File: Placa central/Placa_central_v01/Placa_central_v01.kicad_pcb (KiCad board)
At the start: 2 copper layers, 28 parts, among them J1 Conn_8.4V_PlacaAlimentação, J2 Conn_01x02_ArduinoTxRx, J26 Conn_02x08_Odd_Even, J3 Conn_01x01_ArduinoReset, J37 Conn_01x01_8.4VPonteH, J38 Conn_01x01_5VPonteH, J39 Conn_01x01_GNDPonteH, J4 Conn_GND_PlacaAlimentação, J40 Conn_01x01_Motor1PWM, J41 Conn_01x01_Motor1Dir1, J42 Conn_01x01_Motor1Dir2, J43 Conn_01x01_Motor2Dir1, J44 Conn_01x01_Motor2Dir2, J45 Conn_01x01_Motor2PWM, J48 Conn_01x01_5VEncoderEsq, J49 Conn_01x01_OutputEncoderEsq, J50 Conn_01x01_GNDEncoderEsq, J51 Conn_01x01_5VEncoderDir, J52 Conn_01x01_OutputEncoderDir, J53 Conn_01x01_GNDEncoderDir, SW3 SW_comando1

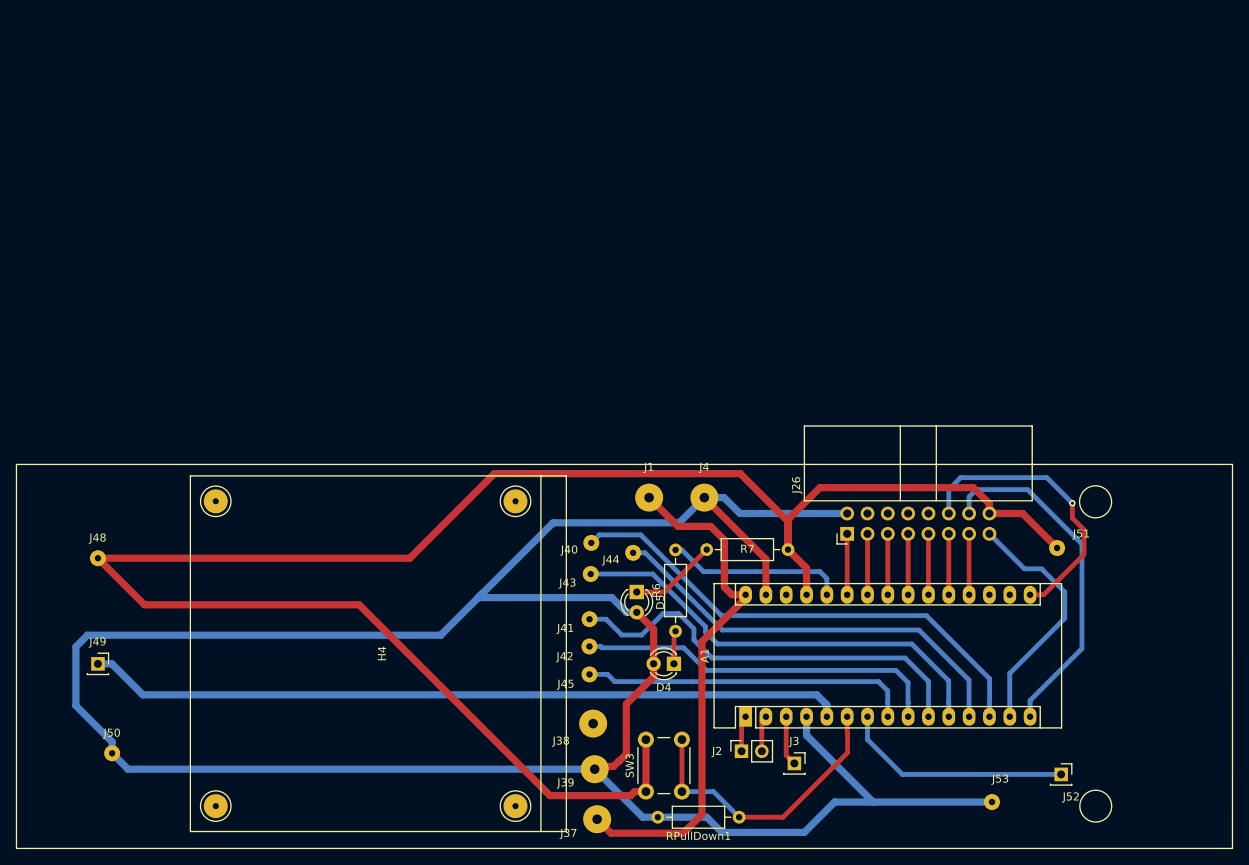
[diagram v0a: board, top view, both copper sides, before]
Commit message: Adicionada a zona de malha de ground, furos pendentes.
A zona de ground ainda não foi preenchida pois os furos da placa para fixação no acrílico requerem atualização.
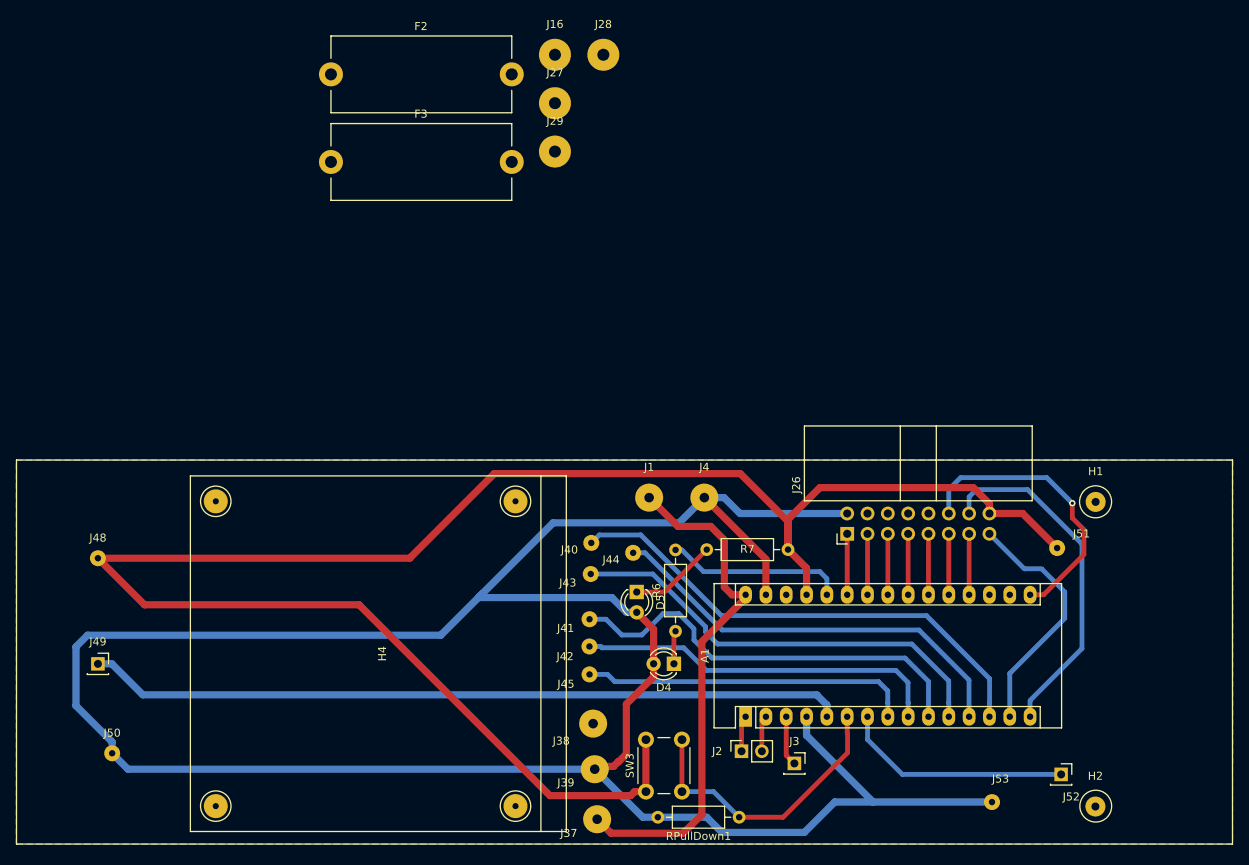
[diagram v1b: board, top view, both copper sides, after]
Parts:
- added F2: Fuse-3A, Fuse:Fuseholder_Cylinder-5x20mm_Stelvio-Kontek_PTF78_Horizontal_Open, F.Cu at (63.9, 74.4)
- added F3: Fuse-3A, Fuse:Fuseholder_Cylinder-5x20mm_Stelvio-Kontek_PTF78_Horizontal_Open, F.Cu at (63.9, 85.3)
- added H1: FuroPlaca, Connector_Wire:SolderWirePad_1x01_Drill1mm, F.Cu at (159.5, 127.8)
- added H2: FuroPlaca, Connector_Wire:SolderWirePad_1x01_Drill1mm, F.Cu at (159.5, 165.9)
- added J16: Conn_01x01_Motor1PonteHPCB, Connector_Wire:SolderWirePad_1x01_Drill1.5mm, F.Cu at (91.9, 71.9)
- added J27: Conn_01x01_Motor2PonteHPCB, Connector_Wire:SolderWirePad_1x01_Drill1.5mm, F.Cu at (91.9, 78.0)
- added J28: Conn_01x01_Motor1PCBMotor, Connector_Wire:SolderWirePad_1x01_Drill1.5mm, F.Cu at (98.0, 71.9)
- added J29: Conn_01x01_Motor2PCBMotor, Connector_Wire:SolderWirePad_1x01_Drill1.5mm, F.Cu at (91.9, 84.0)
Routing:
- added copper zone on B.Cu, net GND

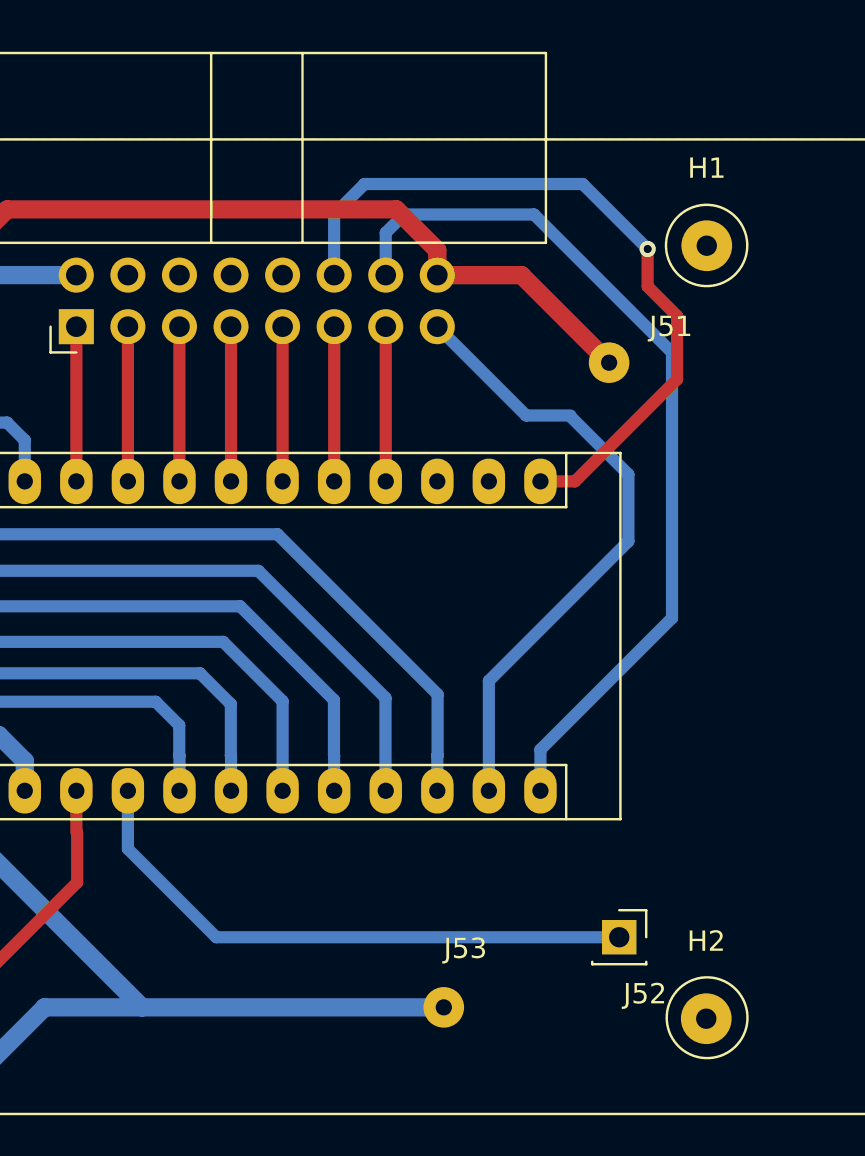
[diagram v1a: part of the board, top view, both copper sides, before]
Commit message: Tamanho dos pinos corrigidos
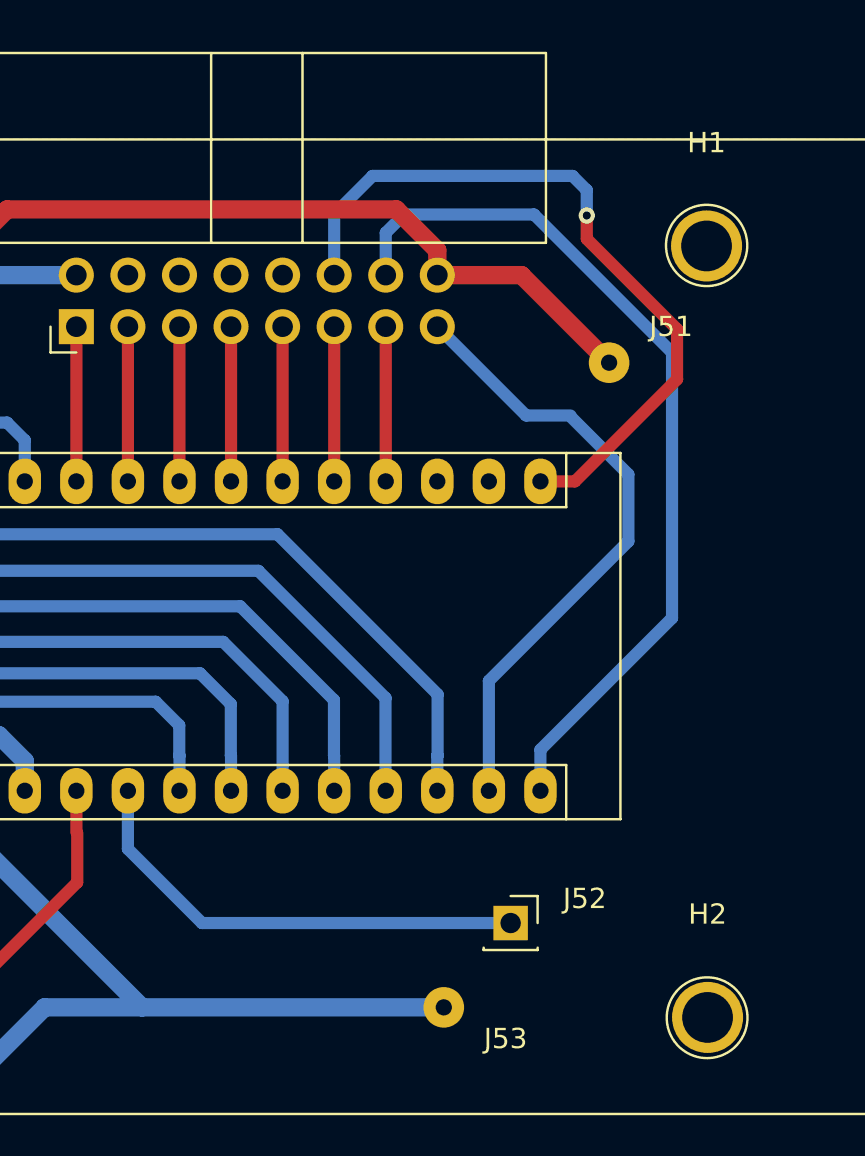
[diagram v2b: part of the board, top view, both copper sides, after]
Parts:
- H1, H2: footprint Connector_Wire:SolderWirePad_1x01_Drill1mm -> Connector_Wire:SolderWirePad_1x01_Drill2.5mm
- moved J52 5.40 mm to (149.8, 161.2)
- moved H2 0.09 mm to (159.6, 165.8)
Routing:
- net Encoder2: track 28.9 -> 23.2 mm
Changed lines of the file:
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@@
-(kicad_pcb (version 20171130) (host pcbnew 5.1.3-ffb9f22~84~ubuntu18.04.1)
+(kicad_pcb (version 20171130) (host pcbnew 5.1.4-e60b266~84~ubuntu18.04.1)
   (general
     (thickness 1.6)
@@
     (mod_text_size 1 1)
     (mod_text_width 0.15)
-    (pad_size 1.524 1.524)
-    (pad_drill 0.762)
+    (pad_size 3.5 3.5)
+    (pad_drill 2.49936)
     (pad_to_mask_clearance 0.051)
     (solder_mask_min_width 0.25)
@@
   )
   (module Connector_PinSocket_2.54mm:PinSocket_1x01_P2.54mm_Vertical (layer F.Cu)
-    (at 155.2 161.9)
+    (at 149.85 161.2)
     (descr "Through hole straight socket strip, 1x01, 2.54mm pitch, single row (from Kicad 4.0.7), script generated")
     (tags "Through hole socket strip THT 1x01 2.54mm single row")
-    (fp_text reference J52 (at 1.27 2.794) (layer F.SilkS)
-      (effects (font (size 1 1) (thickness 0.15)))
-    )
-    (fp_text value Conn_01x01_OutputEncoderDir (at -13.97 0) (layer F.Fab)
-      (effects (font (size 1 1) (thickness 0.15)))
-    )
-    (fp_text user %R (at 0 0) (layer F.Fab)
+    (fp_text reference J52 (at 3.65 -1.2) (layer F.SilkS)
+      (effects (font (size 1 1) (thickness 0.15)))
+    )
+    (fp_text value Conn_01x01_OutputEncoderDir (at 13 -3.25) (layer F.Fab)
+      (effects (font (size 1 1) (thickness 0.15)))
+    )
+    (fp_text user %R (at -0.5 -2.9) (layer F.Fab)
       (effects (font (size 1 1) (thickness 0.15)))
     )
@@
     (tags connector)
     (attr virtual)
-    (fp_text reference J53 (at 1.0668 -2.8956) (layer F.SilkS)
-      (effects (font (size 1 1) (thickness 0.15)))
-    )
-    (fp_text value Conn_01x01_GNDEncoderDir (at 12.4968 0.6604) (layer F.Fab)
+    (fp_text reference J53 (at 3.042 1.546) (layer F.SilkS)
+      (effects (font (size 1 1) (thickness 0.15)))
+    )
+    (fp_text value Conn_01x01_GNDEncoderDir (at -1.908 3.046) (layer F.Fab)
       (effects (font (size 1 1) (thickness 0.15)))
     )
@@
     (fp_line (start -1.5 -1.5) (end -1.5 1.5) (layer F.CrtYd) (width 0.05))
     (fp_line (start -1.5 -1.5) (end 1.5 -1.5) (layer F.CrtYd) (width 0.05))
-    (fp_text user %R (at 1.0668 -2.8956) (layer F.Fab)
+    (fp_text user %R (at 3.192 -0.404) (layer F.Fab)
       (effects (font (size 1 1) (thickness 0.15)))
     )
@@
       (net 40 PCBMotor2_fused))
   )
-  (module Connector_Wire:SolderWirePad_1x01_Drill1mm (layer F.Cu)
-    (at 159.512 127.8382)
-    (descr "Wire solder connection")
-    (tags connector)
-    (attr virtual)
-    (fp_text reference H1 (at 0 -3.81) (layer F.SilkS)
-      (effects (font (size 1 1) (thickness 0.15)))
-    )
-    (fp_text value FuroPlaca (at 0 3.175) (layer F.Fab)
-      (effects (font (size 1 1) (thickness 0.15)))
-    )
-    (fp_line (start 1.75 1.75) (end -1.75 1.75) (layer F.CrtYd) (width 0.05))
-    (fp_line (start 1.75 1.75) (end 1.75 -1.75) (layer F.CrtYd) (width 0.05))
-    (fp_line (start -1.75 -1.75) (end -1.75 1.75) (layer F.CrtYd) (width 0.05))
-    (fp_line (start -1.75 -1.75) (end 1.75 -1.75) (layer F.CrtYd) (width 0.05))
-    (fp_text user %R (at 0 0) (layer F.Fab)
-      (effects (font (size 1 1) (thickness 0.15)))
-    )
-    (pad 1 thru_hole circle (at 0 0) (size 2.49936 2.49936) (drill 1.00076) (layers *.Cu *.Mask))
-  )
-  (module Connector_Wire:SolderWirePad_1x01_Drill1mm (layer F.Cu)
-    (at 159.4866 165.9128)
-    (descr "Wire solder connection")
-    (tags connector)
-    (attr virtual)
-    (fp_text reference H2 (at 0 -3.81) (layer F.SilkS)
-      (effects (font (size 1 1) (thickness 0.15)))
-    )
-    (fp_text value FuroPlaca (at 0 3.175) (layer F.Fab)
-      (effects (font (size 1 1) (thickness 0.15)))
-    )
-    (fp_text user %R (at 0 0) (layer F.Fab)
-      (effects (font (size 1 1) (thickness 0.15)))
-    )
-    (fp_line (start -1.75 -1.75) (end 1.75 -1.75) (layer F.CrtYd) (width 0.05))
-    (fp_line (start -1.75 -1.75) (end -1.75 1.75) (layer F.CrtYd) (width 0.05))
-    (fp_line (start 1.75 1.75) (end 1.75 -1.75) (layer F.CrtYd) (width 0.05))
-    (fp_line (start 1.75 1.75) (end -1.75 1.75) (layer F.CrtYd) (width 0.05))
-    (pad 1 thru_hole circle (at 0 0) (size 2.49936 2.49936) (drill 1.00076) (layers *.Cu *.Mask))
+  (module Connector_Wire:SolderWirePad_1x01_Drill2.5mm (layer F.Cu)
+    (at 159.5 127.85)
+    (descr "Wire solder connection")
+    (tags connector)
+    (attr virtual)
+    (fp_text reference H1 (at 0 -5.08) (layer F.SilkS)
+      (effects (font (size 1 1) (thickness 0.15)))
+    )
+    (fp_text value FuroPlaca (at 0 5.08) (layer F.Fab)
+      (effects (font (size 1 1) (thickness 0.15)))
+    )
+    (fp_line (start 3.5 3.5) (end -3.5 3.5) (layer F.CrtYd) (width 0.05))
+    (fp_line (start 3.5 3.5) (end 3.5 -3.5) (layer F.CrtYd) (width 0.05))
+    (fp_line (start -3.5 -3.5) (end -3.5 3.5) (layer F.CrtYd) (width 0.05))
+    (fp_line (start -3.5 -3.5) (end 3.5 -3.5) (layer F.CrtYd) (width 0.05))
+    (fp_text user %R (at 0 0) (layer F.Fab)
+      (effects (font (size 1 1) (thickness 0.15)))
+    )
+    (pad 1 thru_hole circle (at 0 0) (size 3.5 3.5) (drill 2.49936) (layers *.Cu *.Mask))
+  )
+  (module Connector_Wire:SolderWirePad_1x01_Drill2.5mm (layer F.Cu)
+    (at 159.55 165.85)
+    (descr "Wire solder connection")
+    (tags connector)
+    (attr virtual)
+    (fp_text reference H2 (at 0 -5.08) (layer F.SilkS)
+      (effects (font (size 1 1) (thickness 0.15)))
+    )
+    (fp_text value FuroPlaca (at 0 5.08) (layer F.Fab)
+      (effects (font (size 1 1) (thickness 0.15)))
+    )
+    (fp_text user %R (at 0 0) (layer F.Fab)
+      (effects (font (size 1 1) (thickness 0.15)))
+    )
+    (fp_line (start -3.5 -3.5) (end 3.5 -3.5) (layer F.CrtYd) (width 0.05))
+    (fp_line (start -3.5 -3.5) (end -3.5 3.5) (layer F.CrtYd) (width 0.05))
+    (fp_line (start 3.5 3.5) (end 3.5 -3.5) (layer F.CrtYd) (width 0.05))
+    (fp_line (start 3.5 3.5) (end -3.5 3.5) (layer F.CrtYd) (width 0.05))
+    (pad 1 thru_hole circle (at 0 0) (size 3.5 3.5) (drill 2.49936) (layers *.Cu *.Mask))
   )
   (gr_line (start 24.61768 170.60536) (end 24.61768 122.6019) (layer F.SilkS) (width 0.12))
@@
   (segment (start 125.918 154.686) (end 125.918 153.218) (width 0.9) (layer B.Cu) (net 9))
   (segment (start 138.618 131.826) (end 138.618 139.446) (width 0.6) (layer F.Cu) (net 10))
-  (segment (start 135.347 161.9) (end 155.2 161.9) (width 0.6) (layer B.Cu) (net 11))
   (segment (start 130.998 157.551) (end 130.998 154.686) (width 0.6) (layer B.Cu) (net 11))
-  (segment (start 135.347 161.9) (end 130.998 157.551) (width 0.6) (layer B.Cu) (net 11))
+  (segment (start 134.647 161.2) (end 149.85 161.2) (width 0.6) (layer B.Cu) (net 11))
+  (segment (start 130.998 157.551) (end 134.647 161.2) (width 0.6) (layer B.Cu) (net 11))
   (segment (start 136.078 131.826) (end 136.078 139.446) (width 0.6) (layer F.Cu) (net 12))
   (segment (start 138.618 154.361) (end 138.618 154.686) (width 0.6) (layer B.Cu) (net 13))
@@
   (segment (start 105.6 139.1) (end 110.9 133.8) (width 0.6) (layer F.Cu) (net 30))
   (segment (start 102.15 139.1) (end 105.6 139.1) (width 0.6) (layer F.Cu) (net 30))
+  (via (at 153.6 126.35) (size 0.8) (drill 0.4) (layers F.Cu B.Cu) (net 36))
+  (segment (start 141.158 126.292) (end 141.158 129.286) (width 0.6) (layer B.Cu) (net 36))
+  (segment (start 143.05 124.4) (end 141.158 126.292) (width 0.6) (layer B.Cu) (net 36))
+  (segment (start 152.9 124.4) (end 143.05 124.4) (width 0.6) (layer B.Cu) (net 36))
+  (segment (start 153.6 127.5) (end 153.6 126.35) (width 0.6) (layer F.Cu) (net 36))
+  (segment (start 158.05 131.95) (end 153.6 127.5) (width 0.6) (layer F.Cu) (net 36))
+  (segment (start 158.05 134.414) (end 158.05 131.95) (width 0.6) (layer F.Cu) (net 36))
+  (segment (start 151.318 139.446) (end 153.018 139.446) (width 0.6) (layer F.Cu) (net 36))
   (segment (start 153.018 139.446) (end 158.05 134.414) (width 0.6) (layer F.Cu) (net 36))
-  (segment (start 151.318 139.446) (end 153.018 139.446) (width 0.6) (layer F.Cu) (net 36))
-  (segment (start 158.05 134.414) (end 158.05 131.3) (width 0.6) (layer F.Cu) (net 36))
-  (segment (start 158.05 131.3) (end 156.6 129.85) (width 0.6) (layer F.Cu) (net 36))
-  (segment (start 156.6 129.85) (end 156.6 128) (width 0.6) (layer F.Cu) (net 36))
-  (segment (start 156.6 128) (end 156.6 128) (width 0.6) (layer F.Cu) (net 36))
-  (via (at 156.6 128) (size 0.8) (drill 0.4) (layers F.Cu B.Cu) (net 36))
-  (segment (start 141.158 126.292) (end 141.158 129.286) (width 0.6) (layer B.Cu) (net 36))
-  (segment (start 142.65 124.8) (end 141.158 126.292) (width 0.6) (layer B.Cu) (net 36))
-  (segment (start 156.6 128) (end 153.4 124.8) (width 0.6) (layer B.Cu) (net 36))
-  (segment (start 153.4 124.8) (end 142.65 124.8) (width 0.6) (layer B.Cu) (net 36))
+  (segment (start 153.6 125.1) (end 152.9 124.4) (width 0.6) (layer B.Cu) (net 36))
+  (segment (start 153.6 126.35) (end 153.6 125.1) (width 0.6) (layer B.Cu) (net 36))
   (zone (net 7) (net_name GND) (layer B.Cu) (hatch edge 0.508)
     (connect_pads (clearance 0.508))
